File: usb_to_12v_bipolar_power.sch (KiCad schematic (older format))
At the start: 25 parts, among them J1 USB_A, J2 euro_power_header, J3 USB_5V_out, U1 CC3-0512DF-E

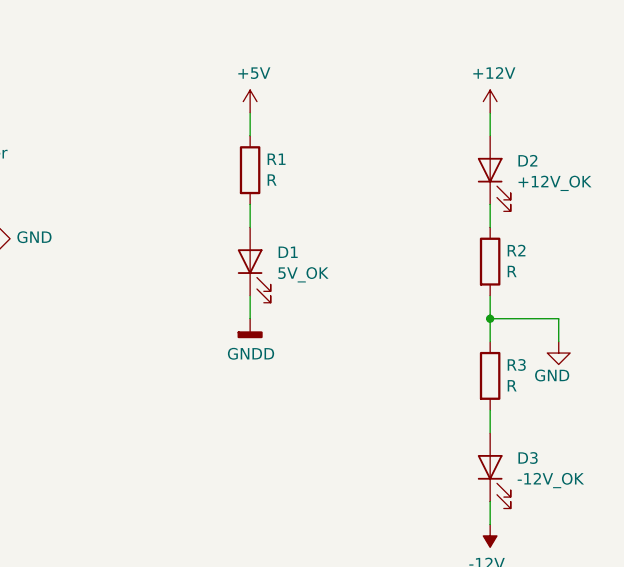
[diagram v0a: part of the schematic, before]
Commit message: add BOM
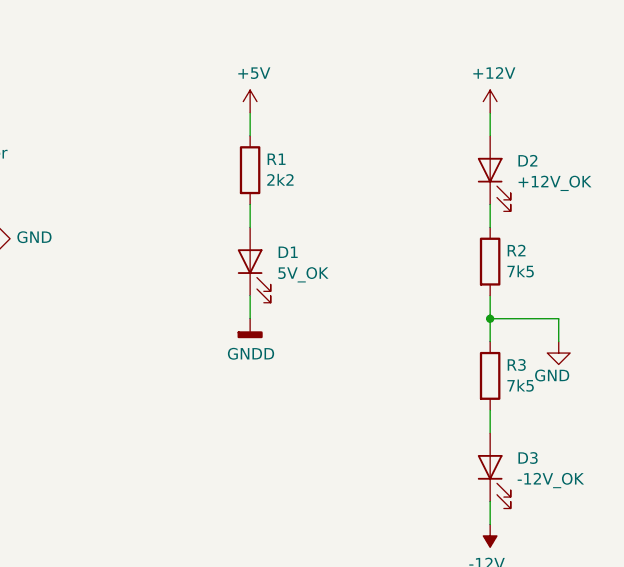
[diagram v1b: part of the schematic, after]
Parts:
- R1: value R -> 2k2
- R2, R3: value R -> 7k5
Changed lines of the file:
@@
 P 8200 3400
 F 0 "R1" H 8270 3446 50  0000 L CNN
-F 1 "R" H 8270 3355 50  0000 L CNN
+F 1 "2k2" H 8270 3355 50  0000 L CNN
 F 2 "Resistor_SMD:R_0805_2012Metric_Pad1.15x1.40mm_HandSolder" V 8130 3400 50  0001 C CNN
 F 3 "~" H 8200 3400 50  0001 C CNN
@@
 P 9250 3800
 F 0 "R2" H 9320 3846 50  0000 L CNN
-F 1 "R" H 9320 3755 50  0000 L CNN
+F 1 "7k5" H 9320 3755 50  0000 L CNN
 F 2 "Resistor_SMD:R_0805_2012Metric_Pad1.15x1.40mm_HandSolder" V 9180 3800 50  0001 C CNN
 F 3 "~" H 9250 3800 50  0001 C CNN
@@
 P 9250 4300
 F 0 "R3" H 9320 4346 50  0000 L CNN
-F 1 "R" H 9320 4255 50  0000 L CNN
+F 1 "7k5" H 9320 4255 50  0000 L CNN
 F 2 "Resistor_SMD:R_0805_2012Metric_Pad1.15x1.40mm_HandSolder" V 9180 4300 50  0001 C CNN
 F 3 "~" H 9250 4300 50  0001 C CNN
